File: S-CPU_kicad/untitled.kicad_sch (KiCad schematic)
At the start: 84 parts

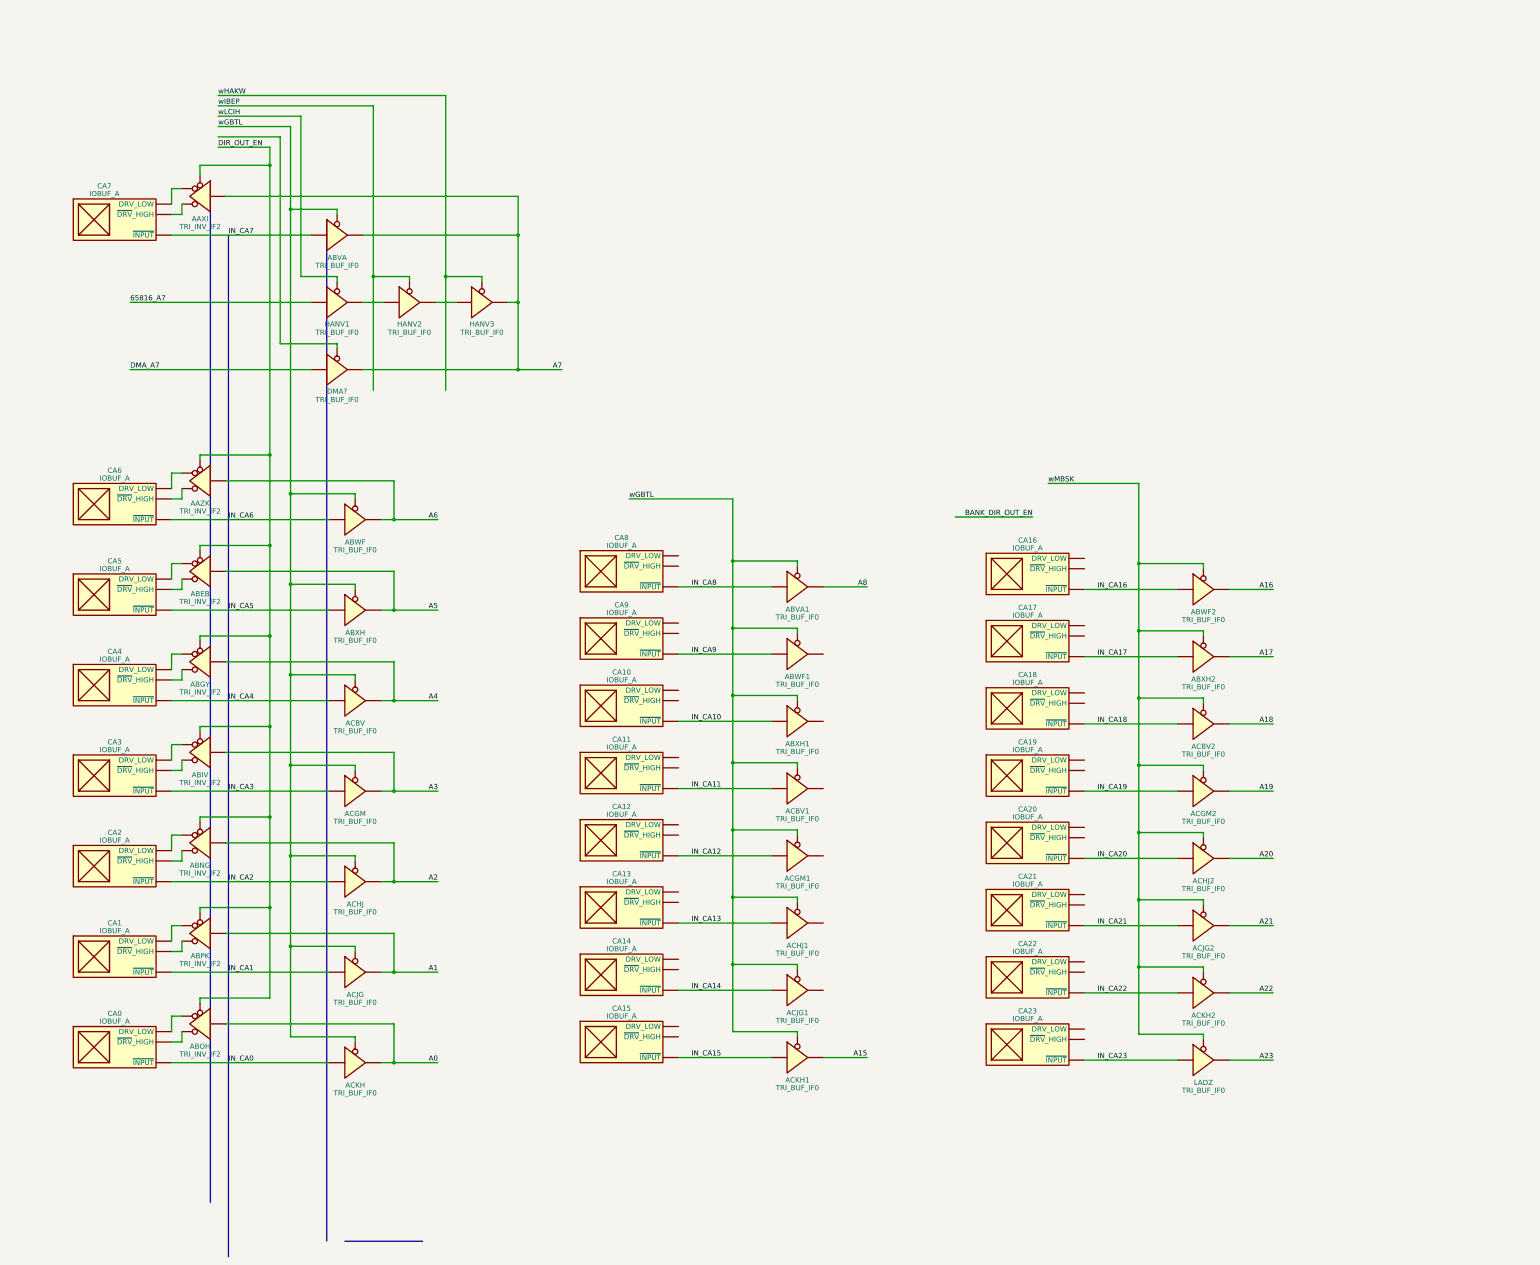
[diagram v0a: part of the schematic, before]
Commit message: Fixed complex gate names. Most fo the cells in the mul div section have been idnetified in SVG file.
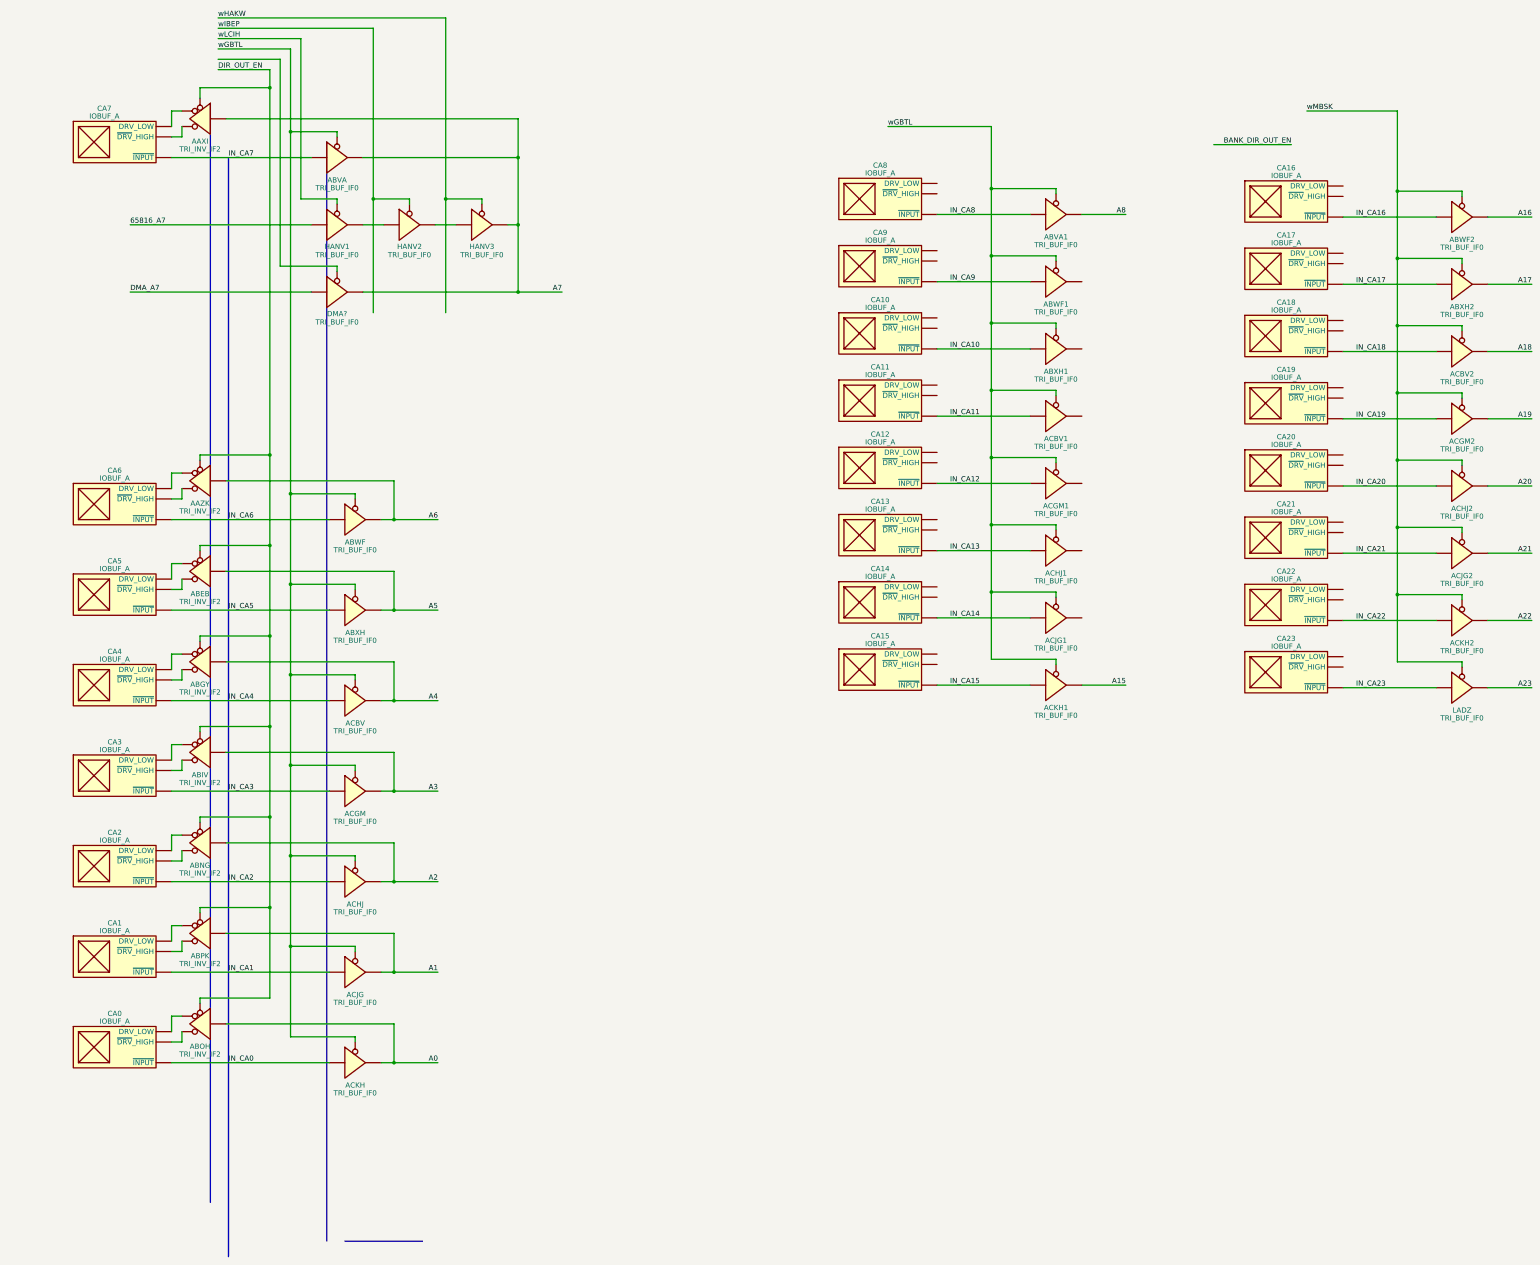
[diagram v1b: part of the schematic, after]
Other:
- moved on the sheet: AAXI, ABVA, ABVA1, ABWF1, ABWF2, ABXH1, ABXH2, ACBV1, ACBV2, ACGM1, ACGM2, ACHJ1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
